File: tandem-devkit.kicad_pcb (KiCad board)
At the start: 4 copper layers, 95.2 x 77.1 mm, 99 parts, among them J101 Conn_01x03, J102 Conn_01x03, J103 Conn_01x06, J104 Conn_01x04, J105 Conn_01x02, J106 QWIIC I2C Connector, J201 PCB Receptacle, J202 PCB Receptacle, J203 Conn_01x06, J301 ConnectorLCDFrontLight, J302 FPC24(0.5MM), J303 FPC10(0.5MM), Q301 2N7002, Q302 2N7002, Q303 AO3401A, U201 AMS1117-ADJ_SOT223

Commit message: PCB: mark logos as not-in-schematic
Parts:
- renumbered G*** to 22uFahrrad-Logo, REF** to BoardOutline, REF** to KiCAD-Logo, REF** to OSHW-Logo
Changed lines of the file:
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@@
   (paper "A4")
   (title_block
-    (title "22  μFahrrad Tandem Devkit")
+    (title "22  uFahrrad Tandem Devkit")
     (date "2022-06-21")
     (rev "0.1")
@@
     (at 140.3 100)
     (attr board_only exclude_from_pos_files exclude_from_bom)
-    (fp_text reference "G***" (at 0 0) (layer "F.SilkS") hide
+    (fp_text reference "22uFahrrad-Logo" (at 0 0) (layer "F.SilkS") hide
       (effects (font (size 1.524 1.524) (thickness 0.3)))
     )
@@
     (at 167.482 59.1465)
     (attr board_only exclude_from_pos_files exclude_from_bom)
-    (fp_text reference "REF**" (at -23.75 -22.502408 unlocked) (layer "F.SilkS") hide
+    (fp_text reference "BoardOutline" (at -23.75 -22.502408 unlocked) (layer "F.SilkS") hide
       (effects (font (size 1 1) (thickness 0.15)))
     )
@@
     (descr "KiCad Logo")
     (tags "Logo KiCad")
-    (attr exclude_from_pos_files exclude_from_bom)
-    (fp_text reference "REF**" (at 0 5.08) (layer "B.SilkS") hide
+    (attr board_only exclude_from_pos_files exclude_from_bom)
+    (fp_text reference "KiCAD-Logo" (at 0 5.08) (layer "B.SilkS") hide
       (effects (font (size 1 1) (thickness 0.15)) (justify mirror))
     )
@@
     (descr "Open Source Hardware Symbol")
     (tags "Logo Symbol OSHW")
-    (attr exclude_from_pos_files exclude_from_bom)
-    (fp_text reference "REF**" (at 0 0) (layer "B.SilkS") hide
+    (attr board_only exclude_from_pos_files exclude_from_bom)
+    (fp_text reference "OSHW-Logo" (at 0 0) (layer "B.SilkS") hide
       (effects (font (size 1 1) (thickness 0.15)) (justify mirror))
     )

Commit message: PCB: add designator for JLC order number
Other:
- board text added: "JLCJLCJLCJLC"
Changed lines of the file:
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@@
     (fp_line (start 1.6 -0.8) (end -1.6 -0.8) (layer "B.Fab") (width 0.1))
     (fp_line (start -1.6 -0.8) (end -1.6 0.8) (layer "B.Fab") (width 0.1))
-    (pad "1" smd roundrect (at -1.475 0 180) (size 1.15 1.8) (layers "B.Cu" "B.Paste" "B.Mask") (roundrect_rratio 0.217391)
+    (pad "1" smd roundrect (at -1.475 0 180) (size 1.15 1.8) (layers "B.Cu" "B.Paste" "B.Mask") (roundrect_rratio 0.2173913043)
       (net 18 "/Display/CP_INT2") (pintype "passive"))
-    (pad "2" smd roundrect (at 1.475 0 180) (size 1.15 1.8) (layers "B.Cu" "B.Paste" "B.Mask") (roundrect_rratio 0.217391)
+    (pad "2" smd roundrect (at 1.475 0 180) (size 1.15 1.8) (layers "B.Cu" "B.Paste" "B.Mask") (roundrect_rratio 0.2173913043)
       (net 19 "/Display/CP_INT1") (pintype "passive"))
     (model "${KICAD6_3DMODEL_DIR}/Capacitor_SMD.3dshapes/C_1206_3216Metric.wrl"
@@
     (fp_line (start -1 0.625) (end 1 0.625) (layer "B.Fab") (width 0.1))
     (fp_line (start -1 -0.625) (end -1 0.625) (layer "B.Fab") (width 0.1))
-    (pad "1" smd roundrect (at -0.9125 0) (size 1.025 1.4) (layers "B.Cu" "B.Paste" "B.Mask") (roundrect_rratio 0.243902)
+    (pad "1" smd roundrect (at -0.9125 0) (size 1.025 1.4) (layers "B.Cu" "B.Paste" "B.Mask") (roundrect_rratio 0.243902439)
       (net 16 "/Display/RESE") (pintype "passive"))
-    (pad "2" smd roundrect (at 0.9125 0) (size 1.025 1.4) (layers "B.Cu" "B.Paste" "B.Mask") (roundrect_rratio 0.243902)
+    (pad "2" smd roundrect (at 0.9125 0) (size 1.025 1.4) (layers "B.Cu" "B.Paste" "B.Mask") (roundrect_rratio 0.243902439)
       (net 41 "/EPD_CURRENT_SENSE") (pintype "passive"))
     (model "${KICAD6_3DMODEL_DIR}/Resistor_SMD.3dshapes/R_0805_2012Metric.wrl"
@@
     (effects (font (size 1 1) (thickness 0.2)) (justify mirror))
   )
+  (gr_text "JLCJLCJLCJLC" (at 191.2 93.4) (layer "B.SilkS")
+    (effects (font (size 1 1) (thickness 0.1524)) (justify mirror))
+  )
   (gr_text "CERN-OHL-S-2.0" (at 149.7 97.3) (layer "B.SilkS")

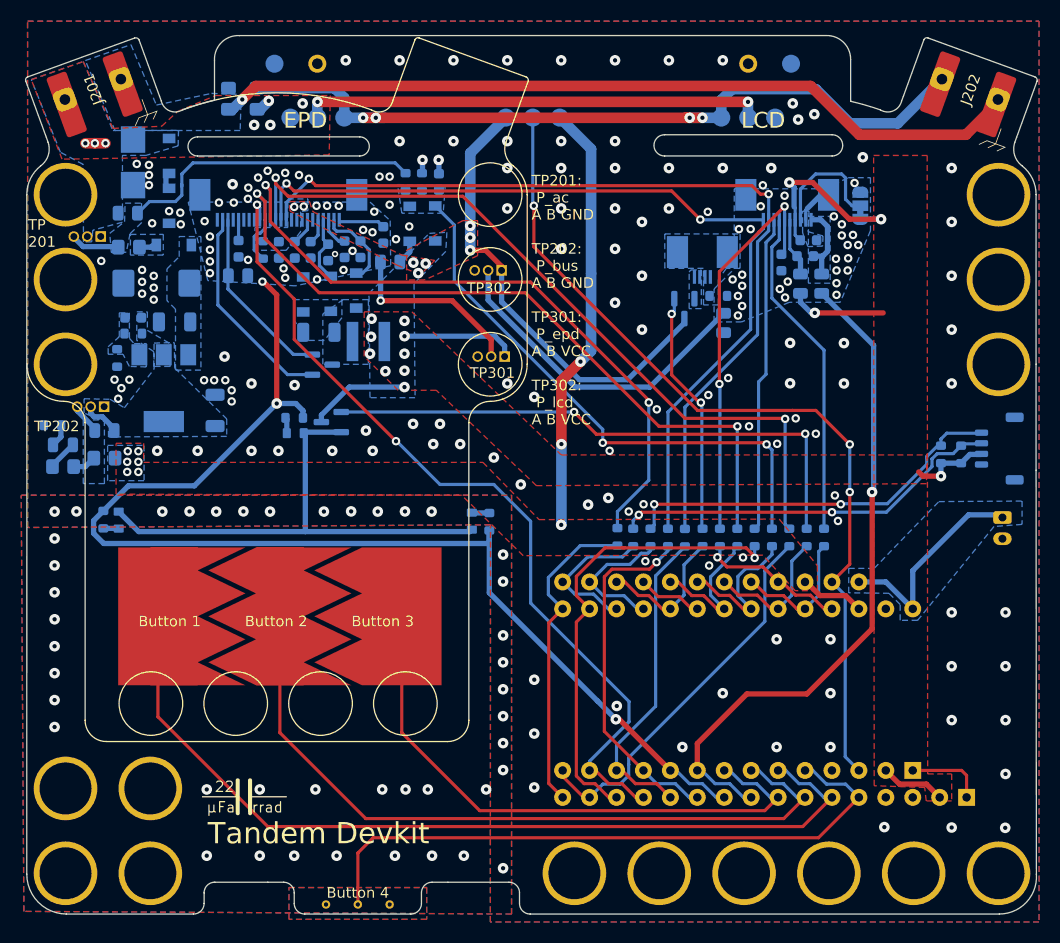
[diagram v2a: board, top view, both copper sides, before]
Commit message: exchange backlight LED for one that is actually white and available
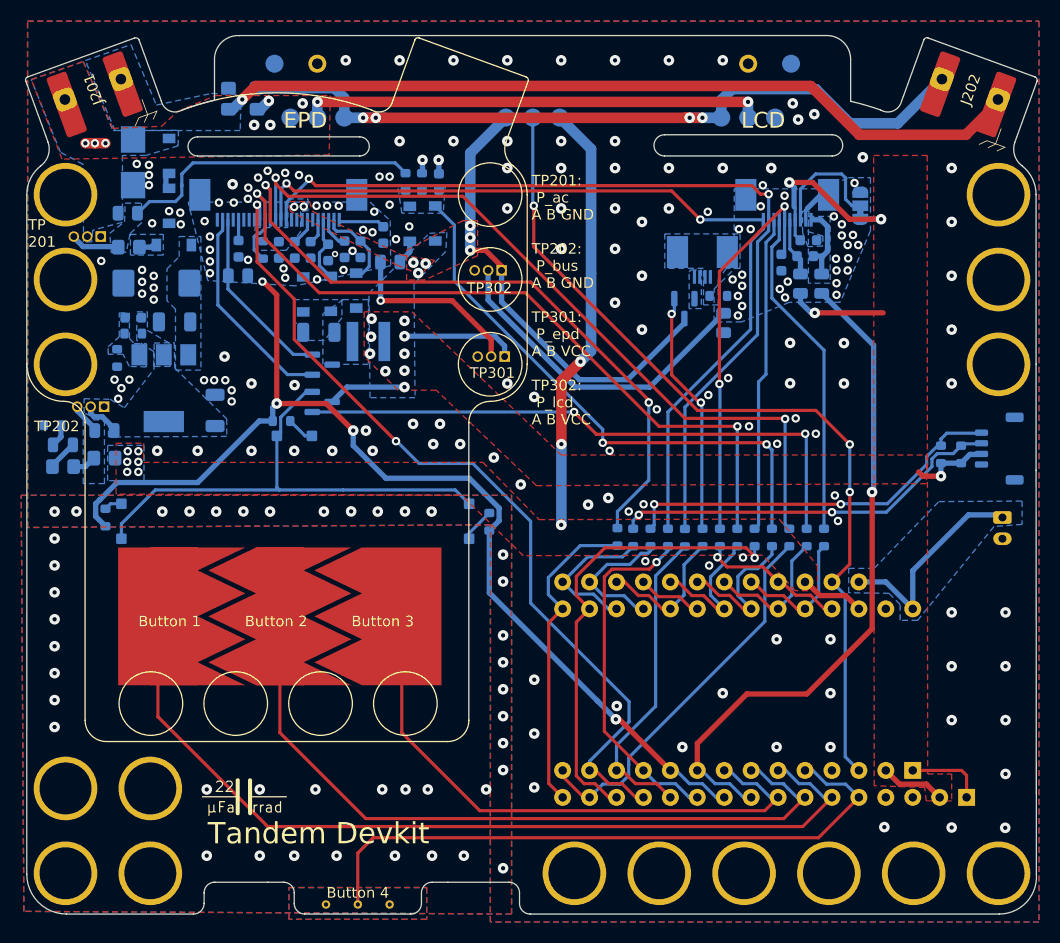
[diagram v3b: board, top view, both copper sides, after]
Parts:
- D301, D302, D303: footprint project-lib:LED_sidemount -> project-lib:LED_sidemount_C205440
- moved Q301 2.09 mm to (147.6, 62.7), turned to 0 degrees
- moved R305 1.24 mm to (143.8, 64.5), turned to 180 degrees
- moved R303 0.28 mm to (127.2, 73.6), turned to -90 degrees
- moved D301 0.17 mm to (128.7, 74.0), turned to -90 degrees
- moved D302 0.15 mm to (145.0, 65.9), turned to 180 degrees
- moved D303 0.12 mm to (161.5, 73.9), turned to 90 degrees
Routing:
- net /EPD_CURRENT_SENSE: track 130.8 -> 118.0 mm, vias 24 -> 25
- net /EPD_BL: track 53.7 -> 56.4 mm
- net VCC: track 104.9 -> 102.7 mm
- net Net-(D303-Pad1): track 1.66 -> 3.22 mm
- net Net-(D302-Pad1): track 1.50 -> 2.62 mm
